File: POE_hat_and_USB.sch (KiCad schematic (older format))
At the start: 93 parts, among them J1 GPIO_CONNECTOR, J2 RJHSE-5385, J3 PIR Motion Sensor, J4 DH22T, J5 USB_A, J8 USB_B_Micro, Q1 DMG1012UW-7, U1 TPS54360B, U2 RTL8152B-VB, U3 FE1.1s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

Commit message: Remove power supply and USB hub.
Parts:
- removed C1, C2: 2.2 µF, Capacitor_SMD:C_1206_3216Metric, symbol Device:C_Small
- removed C11, C13: 47 µF, Capacitor_SMD:C_1210_3225Metric, symbol Device:C_Small
- removed C16, C23, C38: 10 µF, Capacitor_SMD:C_0805_2012Metric, symbol Device:C_Small
- removed C25, C39, C4: 0.1 µF, Capacitor_SMD:C_0402_1005Metric, symbol Device:C_Small
- removed C32, C34: 10 pF, Capacitor_SMD:C_0402_1005Metric, symbol Device:C_Small
- removed C6: 750 pF, Capacitor_SMD:C_0402_1005Metric, symbol Device:C_Small
- removed C8: 27 pF, Capacitor_SMD:C_0402_1005Metric, symbol Device:C_Small
- removed D10: L_USB1, LED_SMD:LED_1206_3216Metric, symbol Device:LED_ALT
- removed D3: B560C, Diode_SMD:D_SMC, symbol Device:D_Schottky
- removed D9: L_USB2, LED_SMD:LED_1206_3216Metric, symbol Device:LED_ALT
- removed J5: USB_A, Connector_USB:USB_A_Molex_67643_Horizontal, symbol Connector:USB_A
- removed L1, L2: 8.2 µH (SRR1210-8R2Y), Inductor_SMD:L_Bourns_SRR1210A, symbol Device:L_Core_Iron
- removed R10: 75k, Resistor_SMD:R_0402_1005Metric, symbol Device:R_Small
- removed R11: 12k, Resistor_SMD:R_0402_1005Metric, symbol Device:R_Small
- removed R21, R22, R23: 100k, Resistor_SMD:R_0402_1005Metric, symbol Device:R_Small
- removed R24, R25, R26: 2.7k, Resistor_SMD:R_0402_1005Metric, symbol Device:R_Small
- removed R3: 520k, Resistor_SMD:R_0402_1005Metric, symbol Device:R_Small
- removed R4: 80, Resistor_SMD:R_0402_1005Metric, symbol Device:R_Small
- removed R5: 150k, Resistor_SMD:R_0402_1005Metric, symbol Device:R_Small
- removed R7: 28.7k, Resistor_SMD:R_0402_1005Metric, symbol Device:R_Small
- removed U1: TPS54360B, Package_SO:TI_SO-PowerPAD-8_ThermalVias, symbol Regulator_Switching:TPS54360DDA
- removed U3: FE1.1s, Package_SO:SSOP-28_3.9x9.9mm_P0.635mm, symbol Interface_USB:FE1.1s
- removed Y1: 12 MHz, Crystal:Crystal_SMD_3225-4Pin_3.2x2.5mm_HandSoldering, symbol Device:Crystal_GND24
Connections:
- net USB_IN+ is gone; now on net USB2+: J8.3 (D+)
- net USB_IN- is gone; now on net USB2-: J8.2 (D-)
- net VDD33: no longer C24.1, C26.1, U2.10 (AVDD33)
- new net: C24.1, C26.1, U2.10 (AVDD33)
- no-connect marks 36 -> 30

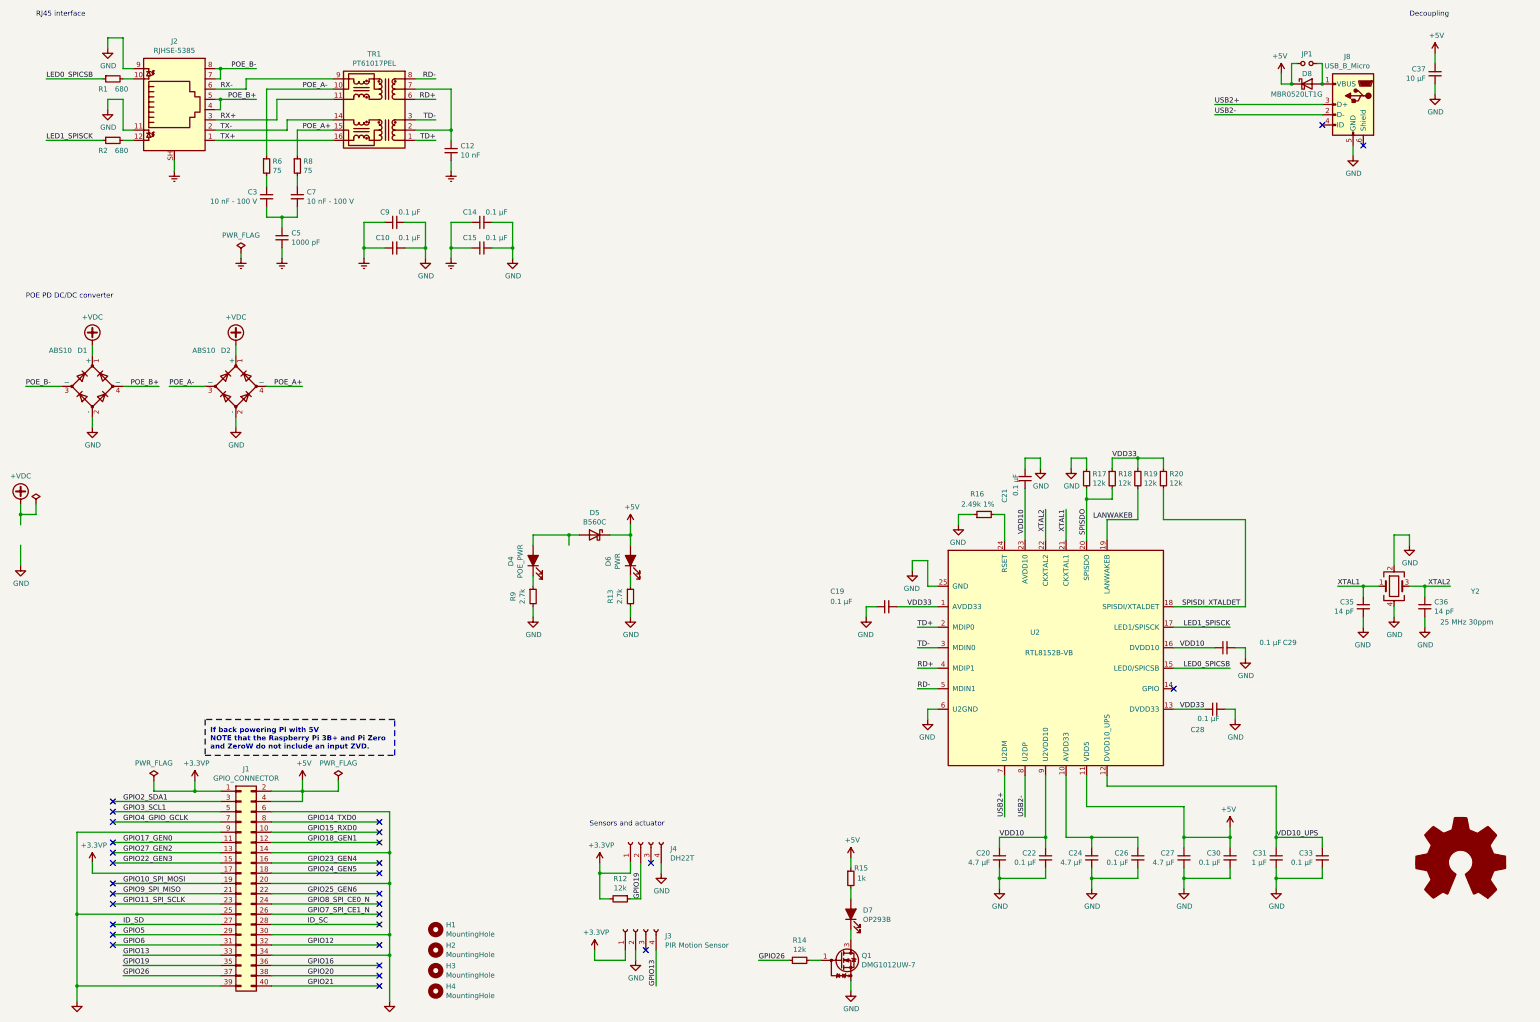
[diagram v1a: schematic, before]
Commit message: Add LM2596HVS to schematic.
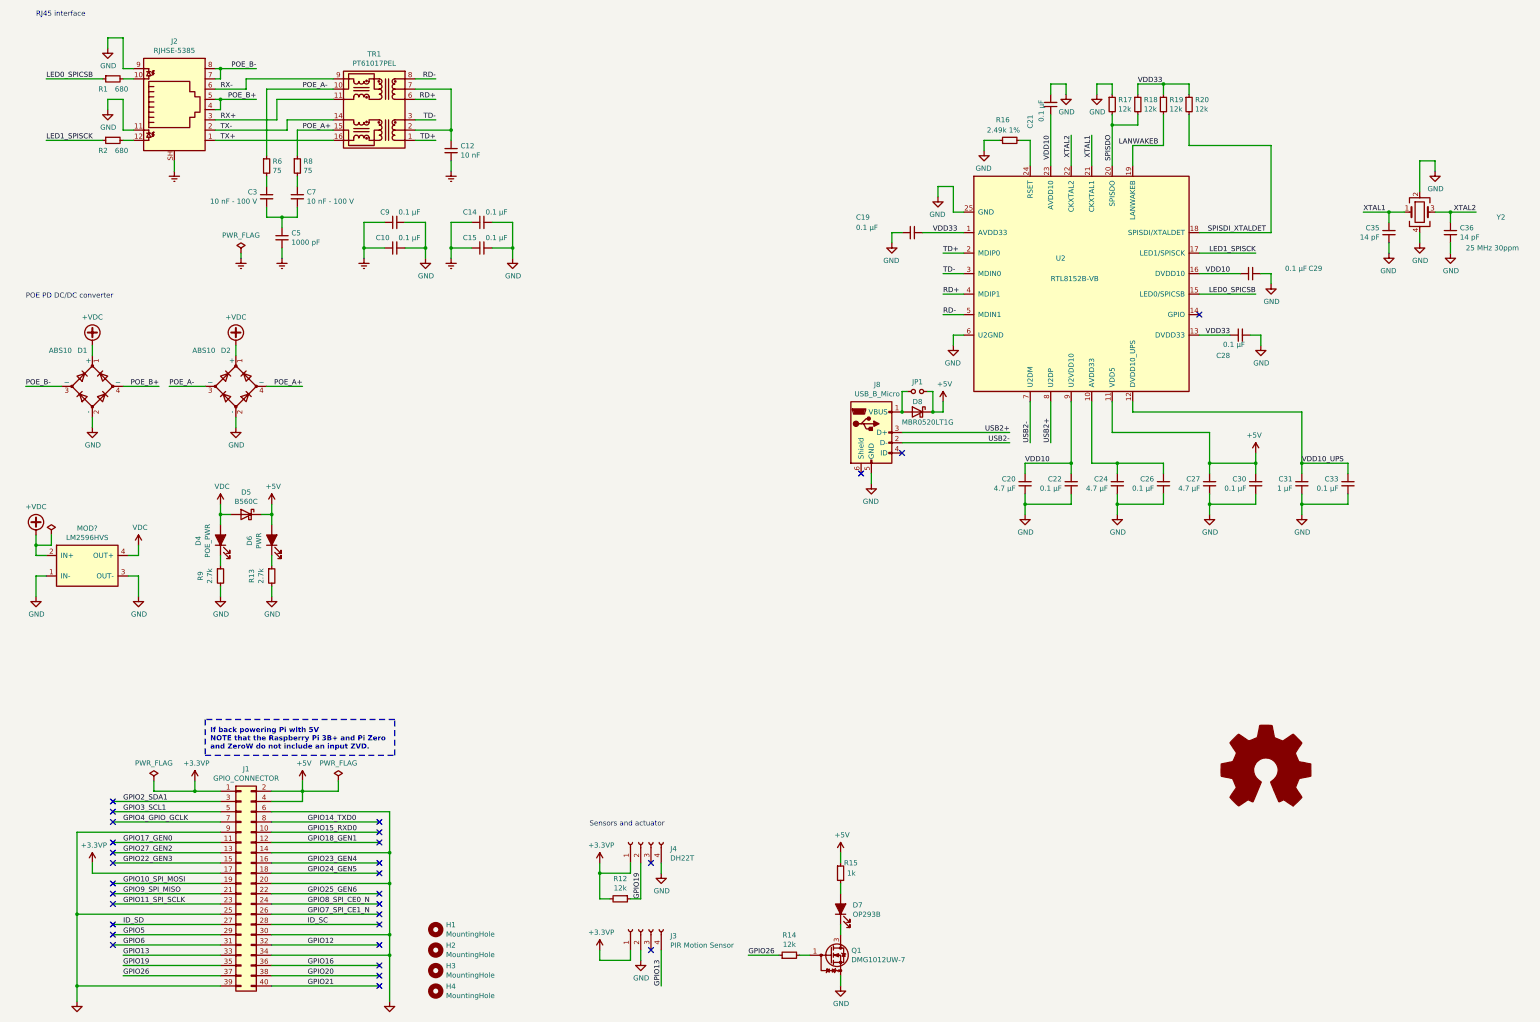
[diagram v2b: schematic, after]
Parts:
- removed C37: 10 µF, Capacitor_SMD:C_0805_2012Metric, symbol Device:C_Small
- added MOD?: LM2596HVS, user-footprints:Module_LM2596HVS, symbol Module_LM2596HVS:LM2596HVS
- D4, D6: footprint LED_SMD:LED_1206_3216Metric -> LED_SMD:LED_0603_1608Metric
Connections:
- net +VDC: now also MOD?.2 (IN+)
- net GND: now also MOD?.1 (IN-), MOD?.3 (OUT-)
- net USB2+: now also U2.8 (U2DP); no longer U2.7 (U2DM)
- net USB2-: now also U2.7 (U2DM); no longer U2.8 (U2DP)
- net VDC: now reaches D4.2 (A), D5.2 (A)
- net VDC: now also MOD?.4 (OUT+)
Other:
- note removed: "Decoupling"
- moved on the sheet: C19, C20, C21, C22, C24, C26, C27, C28, C29, C30, C31, C33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

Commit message: Reroute PCB (removing USB hub, changing power supply and crystal).
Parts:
- Y2: value 25 MHz 30ppm -> 25 MHz 30ppm (HELE(Harmony Elec) X3S025000FC1H-HV); footprint Crystal:Crystal_SMD_3225-4Pin_3.2x2.5mm_HandSoldering -> Crystal:Crystal_SMD_3225-4Pin_3.2x2.5mm
- gave numbers to parts that had none: 1
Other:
- moved on the sheet: C19, C20, C21, C22, C24, C26, C27, C28, C29, C30, C31, C33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
